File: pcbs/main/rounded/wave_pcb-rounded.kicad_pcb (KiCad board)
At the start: 2 copper layers, 114.5 x 95.5 mm, 28 parts

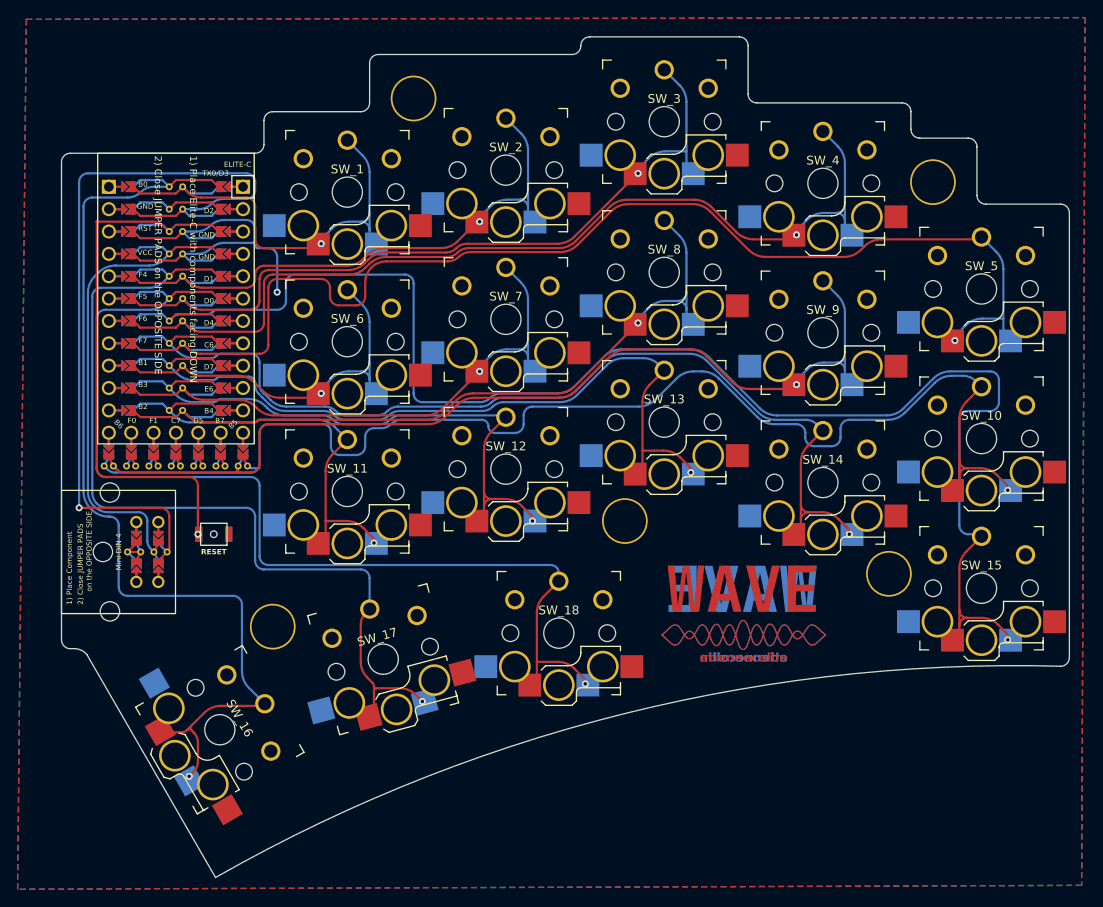
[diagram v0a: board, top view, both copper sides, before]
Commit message: Fixed spacing of PCB edges
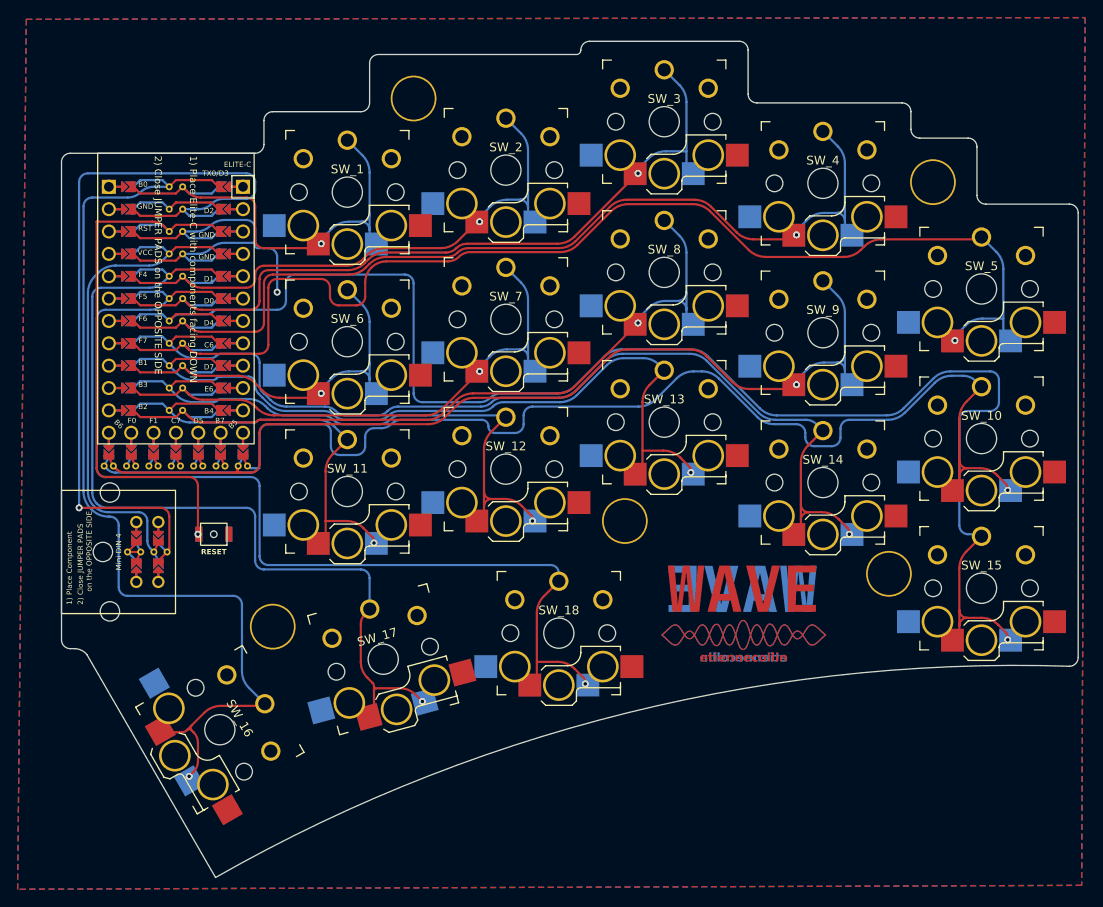
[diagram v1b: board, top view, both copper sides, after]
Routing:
- net Switch14: track 106.1 -> 105.0 mm
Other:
- board size 114.5 x 95.5 mm -> 115.5 x 95 mm
